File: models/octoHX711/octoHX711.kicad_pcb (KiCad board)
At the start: 4 copper layers, 32 x 60 mm, 105 parts, among them J1 Conn_01x04_Male, J10 Conn_01x03_Male, J11 Conn_01x02_Male, J12 Conn_01x03_Male, J2 Conn_01x04_Male, J3 Conn_01x04_Male, J4 Conn_01x04_Male, J5 Conn_01x04_Male, J6 Conn_01x04_Male, J7 Conn_01x04_Male, J8 Conn_01x04_Male, J9 Conn_01x08_Male, Q1 MMBT4403LT1G, Q2 MMBT4403LT1G, Q3 MMBT4403LT1G, Q4 MMBT4403LT1G, Q5 MMBT4403LT1G, Q6 MMBT4403LT1G, Q7 MMBT4403LT1G, Q8 MMBT4403LT1G, U1 HX711, U2 HX711, U3 HX711, U4 HX711, U5 HX711, U6 HX711, U7 HX711, U8 HX711

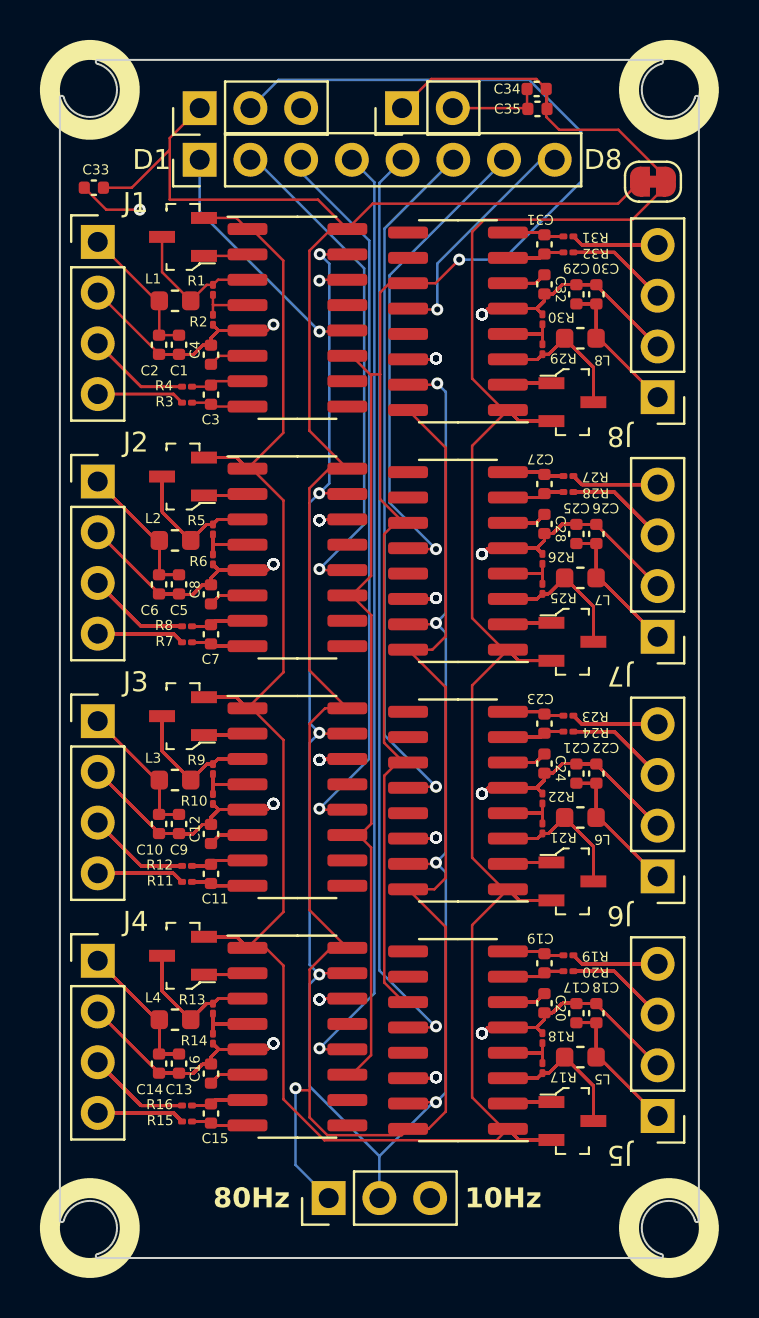
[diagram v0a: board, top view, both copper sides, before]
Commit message: fixed silkscreen and added arduino lib
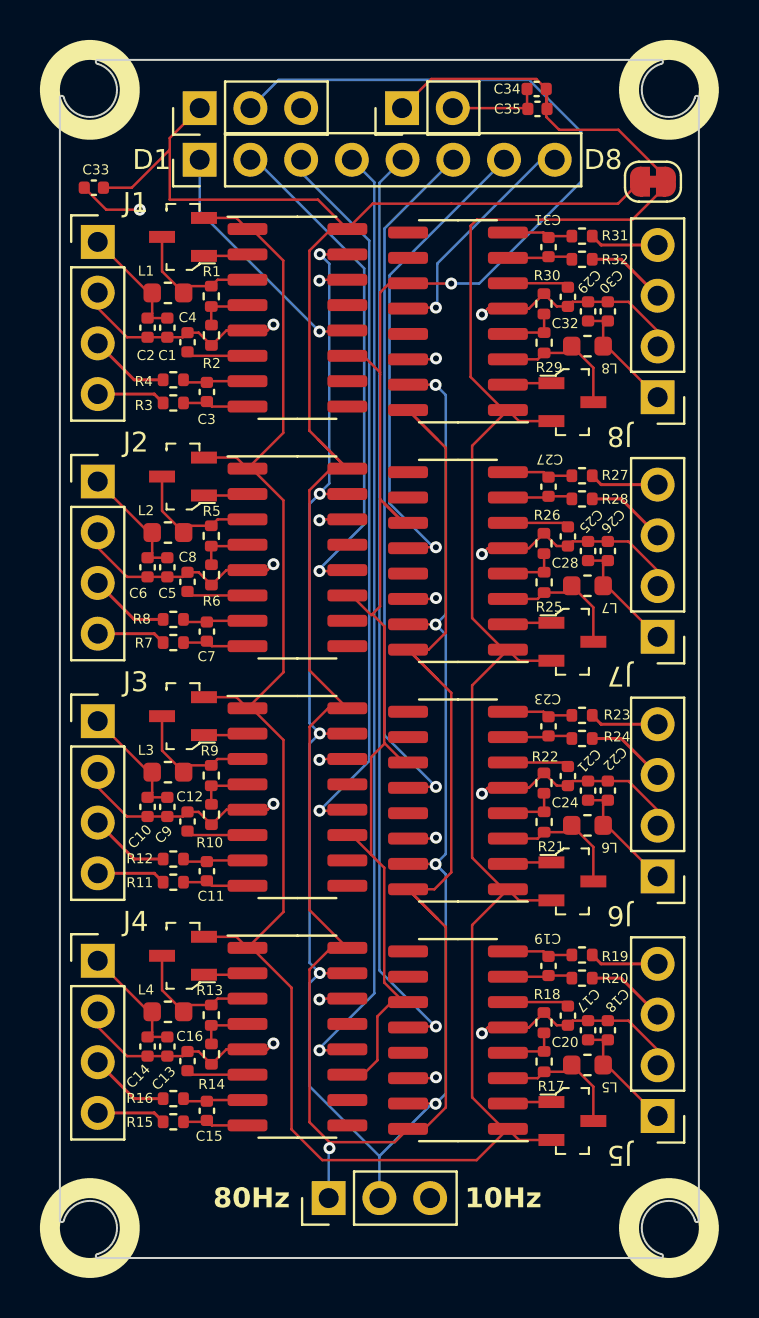
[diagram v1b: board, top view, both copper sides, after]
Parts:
- R1, R10, R11, R12, R13, R14, R15, R16, R17, R18, R19, R2, R20, R21, R22, R23, R24, R25, R26, R27, R28, R29, R3, R30, R31, R32, R4, R5, R6, R7, R8, R9: footprint Resistor_SMD:R_01005_0402Metric -> Resistor_SMD:R_0402_1005Metric
- moved C12 1.33 mm to (131.4, 103.1)
- moved C16 1.33 mm to (131.4, 115.1)
- moved C20 1.33 mm to (150.4, 112.9)
- moved C24 1.33 mm to (150.4, 100.9)
- moved C28 1.33 mm to (150.4, 88.9)
- moved C32 1.33 mm to (150.4, 76.9)
- moved C4 1.33 mm to (131.4, 79.1)
- moved C8 1.33 mm to (131.4, 91.1)
- moved C1 1.04 mm to (130.4, 78.4)
- moved C13 1.04 mm to (130.4, 114.4)
- moved C5 1.04 mm to (130.4, 90.4)
- moved C9 1.04 mm to (130.4, 102.4)
- moved C17 1.04 mm to (151.4, 113.6)
- moved C21 1.04 mm to (151.4, 101.6)
- moved C25 1.04 mm to (151.4, 89.6)
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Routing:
- net GND: track 3031.0 -> 107.1 mm, vias 73 -> 17
- net VCC: track 396.9 -> 162.0 mm
- net /HX711_unit6/avdd: track 106.1 -> 6.72 mm
- net /HX711_unit8/avdd: track 106.1 -> 6.72 mm
- net /HX711_unit7/avdd: track 106.1 -> 6.72 mm
- net /HX711_unit5/avdd: track 106.1 -> 6.72 mm
- net /HX711_unit2/avdd: track 106.1 -> 6.72 mm
- net /HX711_unit3/avdd: track 106.1 -> 6.72 mm
- net /HX711_unit4/avdd: track 106.1 -> 6.72 mm
- net /HX711_unit8/a-in: track 43.4 -> 3.28 mm
- net /HX711_unit6/a-in: track 43.4 -> 3.28 mm
- net /HX711_unit7/a-in: track 43.4 -> 3.28 mm
- net /HX711_unit5/a-in: track 43.4 -> 3.28 mm
- net /HX711_unit4/a-in: track 43.4 -> 3.28 mm
- net /HX711_unit3/a-in: track 43.4 -> 3.28 mm
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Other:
- board text removed: "e-"
